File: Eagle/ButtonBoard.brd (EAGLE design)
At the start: 100 x 80 mm, 8 parts

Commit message: - some modifications, corrections, ...
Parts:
- added LED1: Yellow, led:LED3MM
- added LED2: Red, led:LED3MM
- added R3: 470R, rcl:0207/10
- added R4: 820R, rcl:0207/10
- R1, R2: value (none) -> 470R
- X1: device con-molex:KK-156-8 -> con-molex:KK-156-10
- moved X1 73.8 mm to (-25.4, -25.4)
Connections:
- new net N$11: LED2.A, R4.1
- new net N$12: LED1.A, R3.2
- new net N$13: R3.1, X1.2
- new net N$14: R4.2, X1.1
- net GND: now also LED1.K, LED2.K, X1.10; no longer X1.1
- net N$2: now also X1.3; no longer X1.8
- net N$3: now also X1.4; no longer X1.7
- net N$4: now also X1.9; no longer X1.2
- net N$6: now also X1.8; no longer X1.3
- net N$7: now also X1.7; no longer X1.4
- net N$8: now also X1.6; no longer X1.5
- net N$9: now also X1.5; no longer X1.6
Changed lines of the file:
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@@
 <element name="S2" library="switch" package="REKN" value="" x="-20.32" y="7.62"/>
 <element name="S3" library="switch" package="REKN" value="" x="-35.56" y="7.62"/>
-<element name="R1" library="rcl" package="0207/10" value="" x="-19.05" y="54.61"/>
-<element name="R2" library="rcl" package="0207/10" value="" x="-31.75" y="54.61"/>
+<element name="R1" library="rcl" package="0207/10" value="470R" x="-19.05" y="54.61"/>
+<element name="R2" library="rcl" package="0207/10" value="470R" x="-31.75" y="54.61"/>
 <element name="S5" library="switch" package="5501-1LED" value="5501-1LED" x="-21.59" y="36.83"/>
 <element name="S1" library="switch" package="5501-1LED" value="5501-1LED" x="-36.83" y="21.59"/>
-<element name="X1" library="con-molex" package="KK-156-8" value="" x="-29.21" y="48.26">
-<attribute name="OC_NEWARK" value="unknown" x="0" y="0" size="1.778" layer="27" display="off"/>
-<attribute name="MPN" value="" x="0" y="0" size="1.778" layer="27" display="off"/>
-<attribute name="MF" value="" x="0" y="0" size="1.778" layer="27" display="off"/>
-<attribute name="OC_FARNELL" value="unknown" x="0" y="0" size="1.778" layer="27" display="off"/>
+<element name="R3" library="rcl" package="0207/10" value="470R" x="-40.64" y="-3.81"/>
+<element name="R4" library="rcl" package="0207/10" value="820R" x="-40.64" y="-8.89"/>
+<element name="LED1" library="led" package="LED3MM" value="Yellow" x="-44.45" y="-12.7"/>
+<element name="LED2" library="led" package="LED3MM" value="Red" x="-44.45" y="-17.78"/>
+<element name="X1" library="con-molex" package="KK-156-10" value="" x="-25.4" y="-25.4">
+<attribute name="OC_NEWARK" value="unknown" x="-25.4" y="-25.4" size="1.778" layer="27" display="off"/>
+<attribute name="MPN" value="" x="-25.4" y="-25.4" size="1.778" layer="27" display="off"/>
+<attribute name="MF" value="" x="-25.4" y="-25.4" size="1.778" layer="27" display="off"/>
+<attribute name="OC_FARNELL" value="unknown" x="-25.4" y="-25.4" size="1.778" layer="27" display="off"/>
 </element>
 </elements>
 <signals>
 <signal name="GND">
-<contactref element="X1" pad="1"/>
 <contactref element="S5" pad="-"/>
 <contactref element="S1" pad="-"/>
@@
 <contactref element="S4" pad="0B"/>
 <contactref element="S1" pad="1B"/>
+<contactref element="LED1" pad="K"/>
+<contactref element="LED2" pad="K"/>
+<contactref element="X1" pad="10"/>
+<wire x1="-43.18" y1="-12.7" x2="-43.18" y2="-17.78" width="0" layer="19" extent="1-1"/>
+<wire x1="-30.48" y1="2.54" x2="-43.18" y2="-12.7" width="0" layer="19" extent="1-1"/>
 <wire x1="-15.24" y1="2.54" x2="-30.48" y2="2.54" width="0" layer="19" extent="1-1"/>
 <wire x1="-15.24" y1="17.78" x2="-15.24" y2="2.54" width="0" layer="19" extent="1-1"/>
@@
 <wire x1="-21.59" y1="33.02" x2="-15.24" y2="17.78" width="0" layer="19" extent="1-1"/>
 <wire x1="-26.67" y1="40.64" x2="-21.59" y2="33.02" width="0" layer="19" extent="1-1"/>
-<wire x1="-43.07" y1="48.26" x2="-26.67" y2="40.64" width="0" layer="19" extent="1-1"/>
+<wire x1="-7.58" y1="-25.4" x2="-15.24" y2="2.54" width="0" layer="19" extent="1-1"/>
 </signal>
 <signal name="N$2">
 <contactref element="R2" pad="1"/>
-<contactref element="X1" pad="8"/>
-<wire x1="-36.83" y1="54.61" x2="-15.35" y2="48.26" width="0" layer="19" extent="1-1"/>
+<contactref element="X1" pad="3"/>
+<wire x1="-36.83" y1="54.61" x2="-35.3" y2="-25.4" width="0" layer="19" extent="1-1"/>
 </signal>
 <signal name="N$3">
 <contactref element="R1" pad="1"/>
-<contactref element="X1" pad="7"/>
-<wire x1="-19.31" y1="48.26" x2="-24.13" y2="54.61" width="0" layer="19" extent="1-1"/>
+<contactref element="X1" pad="4"/>
+<wire x1="-24.13" y1="54.61" x2="-31.34" y2="-25.4" width="0" layer="19" extent="1-1"/>
 </signal>
 <signal name="N$1">
@@
 <signal name="N$4">
 <contactref element="S5" pad="NO"/>
-<contactref element="X1" pad="2"/>
-<wire x1="-39.11" y1="48.26" x2="-16.51" y2="40.64" width="0" layer="19" extent="1-1"/>
+<contactref element="X1" pad="9"/>
+<wire x1="-16.51" y1="40.64" x2="-11.54" y2="-25.4" width="0" layer="19" extent="1-1"/>
 </signal>
 <signal name="N$6">
 <contactref element="S2" pad="1B"/>
-<contactref element="X1" pad="3"/>
-<wire x1="-35.15" y1="48.26" x2="-20.32" y2="2.54" width="0" layer="19" extent="1-1"/>
+<contactref element="X1" pad="8"/>
+<wire x1="-20.32" y1="2.54" x2="-15.5" y2="-25.4" width="0" layer="19" extent="1-1"/>
 </signal>
 <signal name="N$7">
-<contactref element="X1" pad="4"/>
 <contactref element="S3" pad="1B"/>
-<wire x1="-31.19" y1="48.26" x2="-35.56" y2="2.54" width="0" layer="19" extent="1-1"/>
+<contactref element="X1" pad="7"/>
+<wire x1="-35.56" y1="2.54" x2="-19.46" y2="-25.4" width="0" layer="19" extent="1-1"/>
 </signal>
 <signal name="N$8">
-<contactref element="X1" pad="5"/>
 <contactref element="S4" pad="1B"/>
-<wire x1="-20.32" y1="17.78" x2="-27.23" y2="48.26" width="0" layer="19" extent="1-1"/>
+<contactref element="X1" pad="6"/>
+<wire x1="-20.32" y1="17.78" x2="-23.42" y2="-25.4" width="0" layer="19" extent="1-1"/>
 </signal>
 <signal name="N$9">
-<contactref element="X1" pad="6"/>
 <contactref element="S1" pad="NO"/>
-<wire x1="-31.75" y1="25.4" x2="-23.27" y2="48.26" width="0" layer="19" extent="1-1"/>
+<contactref element="X1" pad="5"/>
+<wire x1="-31.75" y1="25.4" x2="-27.38" y2="-25.4" width="0" layer="19" extent="1-1"/>
+</signal>
+<signal name="N$11">
+<contactref element="LED2" pad="A"/>
+<contactref element="R4" pad="1"/>
+<wire x1="-45.72" y1="-8.89" x2="-45.72" y2="-17.78" width="0" layer="19" extent="1-1"/>
+</signal>
+<signal name="N$12">
+<contactref element="LED1" pad="A"/>
+<contactref element="R3" pad="2"/>
+<wire x1="-35.56" y1="-3.81" x2="-45.72" y2="-12.7" width="0" layer="19" extent="1-1"/>
+</signal>
+<signal name="N$13">
+<contactref element="X1" pad="2"/>
+<contactref element="R3" pad="1"/>
+<wire x1="-45.72" y1="-3.81" x2="-39.26" y2="-25.4" width="0" layer="19" extent="1-1"/>
+</signal>
+<signal name="N$14">
+<contactref element="R4" pad="2"/>
+<contactref element="X1" pad="1"/>
+<wire x1="-35.56" y1="-8.89" x2="-43.22" y2="-25.4" width="0" layer="19" extent="1-1"/>
 </signal>
 </signals>

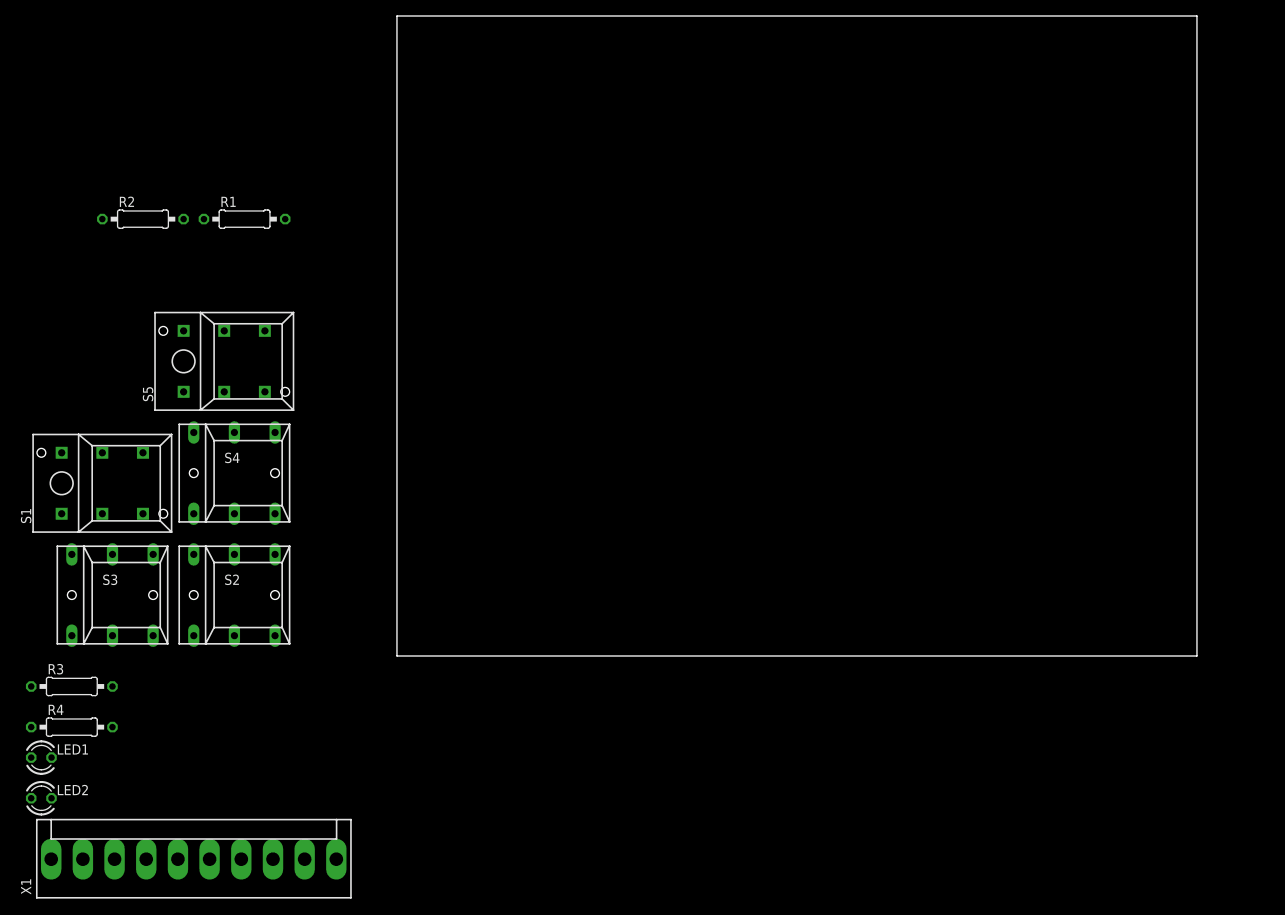
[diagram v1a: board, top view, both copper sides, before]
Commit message: - corrections for RelayBoard1:   - using right connectors from library con-molex   - single sided routing - corrections for ButtonBoard:   - using right connector from library con-molex   - using right switches from library switch-misc (SRK/SRKL) - component placement & board layout for ButtonBoard done - CPUBoard:   - some components moved around the board   - re-routing (partially)
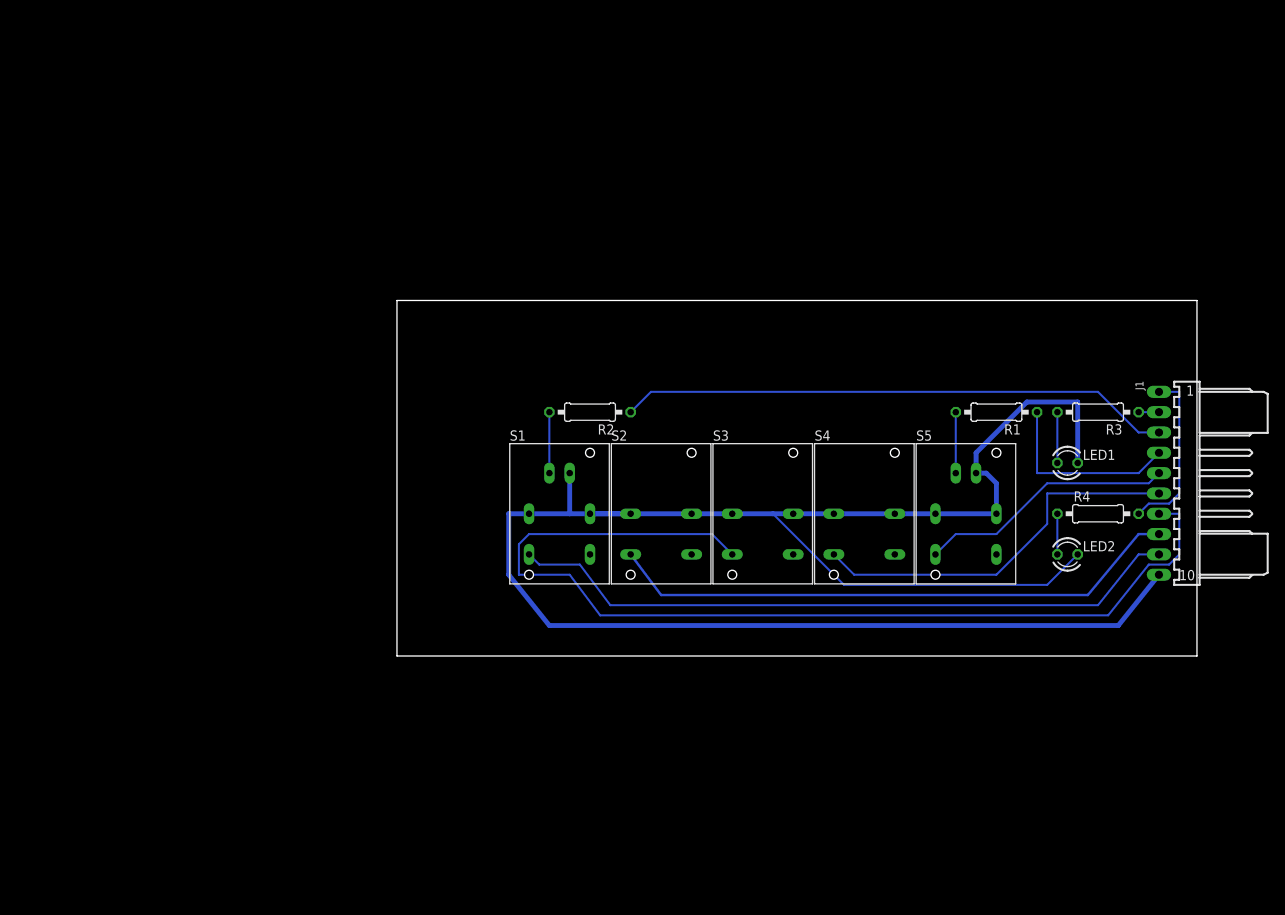
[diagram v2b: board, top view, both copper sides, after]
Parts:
- removed X1: (no value), con-molex:KK-156-10
- added J1: CPU_BOARD, con-molex:7395-10
- S1, S5: value 5501-1LED -> SRKL; device switch:5501-1LED -> switch-misc:SRKL
- S2, S3, S4: value (none) -> SRK; device switch:REKN -> switch-misc:SRK
- moved LED1 133.5 mm to (83.8, 24.1)
- moved R3 132.8 mm to (87.6, 30.5), turned to 180 degrees
- moved LED2 131.8 mm to (83.8, 12.7)
- moved R4 131.0 mm to (87.6, 17.8)
- moved R1 97.0 mm to (74.9, 30.5), turned to 180 degrees
- moved S5 94.6 mm to (71.1, 17.8)
- moved S3 81.9 mm to (45.7, 17.8)
- moved S4 78.9 mm to (58.4, 17.8)
- moved R2 60.9 mm to (24.1, 30.5), turned to 180 degrees
- moved S1 57.3 mm to (20.3, 17.8)
- moved S2 54.3 mm to (33.0, 17.8)
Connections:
- net GND: now also J1.10, S1.2, S1.3, S2.2, S2.3, S3.2, S3.3, S4.2, S4.3, S5.2, S5.3; no longer S1.1B, S2.0B, S3.0B, S4.0B, S5.1B, X1.10
- net N$1: now also S1.+; no longer S5.+
- net N$13: now also J1.2; no longer X1.2
- net N$14: now also J1.1; no longer X1.1
- net N$2: now also J1.3; no longer X1.3
- net N$3: now also J1.4; no longer X1.4
- net N$4: now also J1.9, S1.1; no longer S5.NO, X1.9
- net N$5: now also S5.+; no longer S1.+
- net N$6: now also J1.8, S2.1; no longer S2.1B, X1.8
- net N$7: now also J1.7, S3.1; no longer S3.1B, X1.7
- net N$8: now also J1.6, S4.1; no longer S4.1B, X1.6
- net N$9: now also J1.5, S5.1; no longer S1.NO, X1.5
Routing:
- net GND: track 0.00 -> 241.9 mm
- net N$7: track 0.00 -> 128.3 mm
- net N$4: track 0.00 -> 84.9 mm
- net N$6: track 0.00 -> 72.1 mm
- net N$2: track 0.00 -> 69.2 mm
- net N$8: track 0.00 -> 48.1 mm
- net N$9: track 0.00 -> 32.1 mm
- net N$3: track 0.00 -> 23.9 mm
- net N$14: track 0.00 -> 21.4 mm
- net N$5: track 0.00 -> 7.62 mm
- net N$1: track 0.00 -> 7.62 mm
- net N$12: track 0.00 -> 6.35 mm
- net N$11: track 0.00 -> 5.08 mm
- net N$13: track 0.00 -> 2.54 mm
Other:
- board size 100 x 80 mm -> 100 x 44.4 mm
